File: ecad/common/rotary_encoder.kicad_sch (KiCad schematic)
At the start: 7 parts, among them Q1 RE1C002UN, SW1 PEL12T, U1 TLC5973

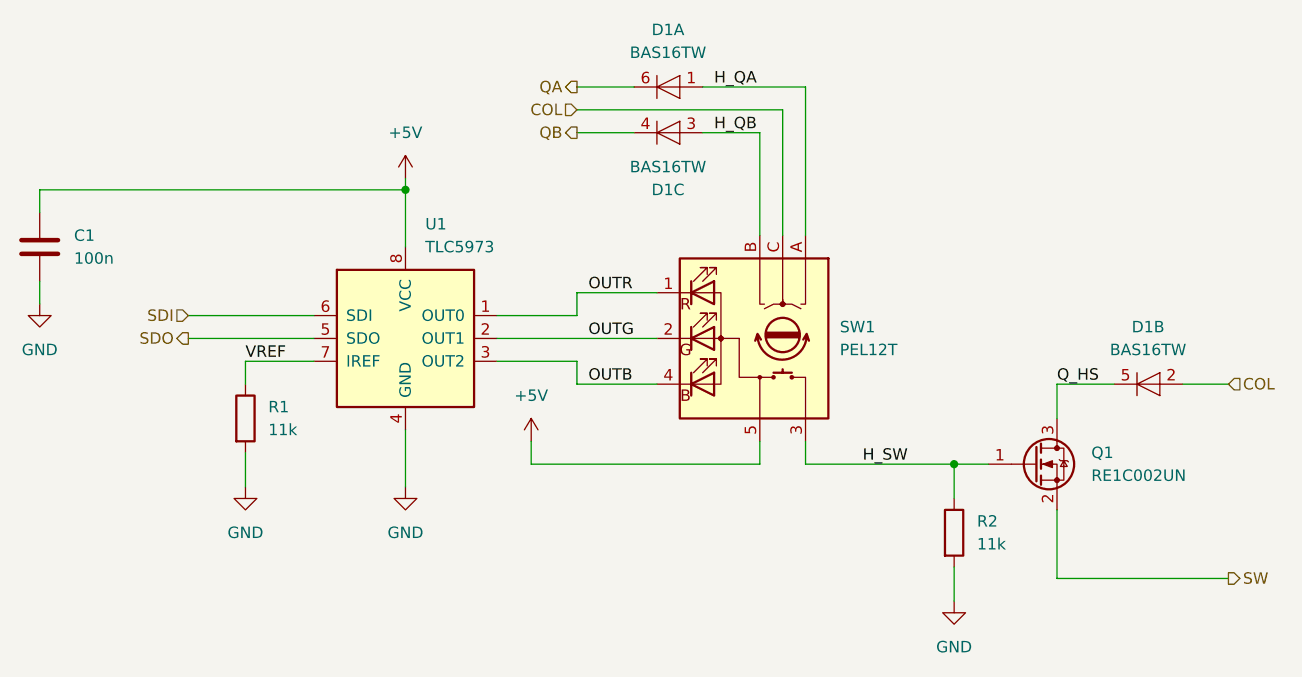
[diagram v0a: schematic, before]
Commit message: Draft a slightly smaller top board
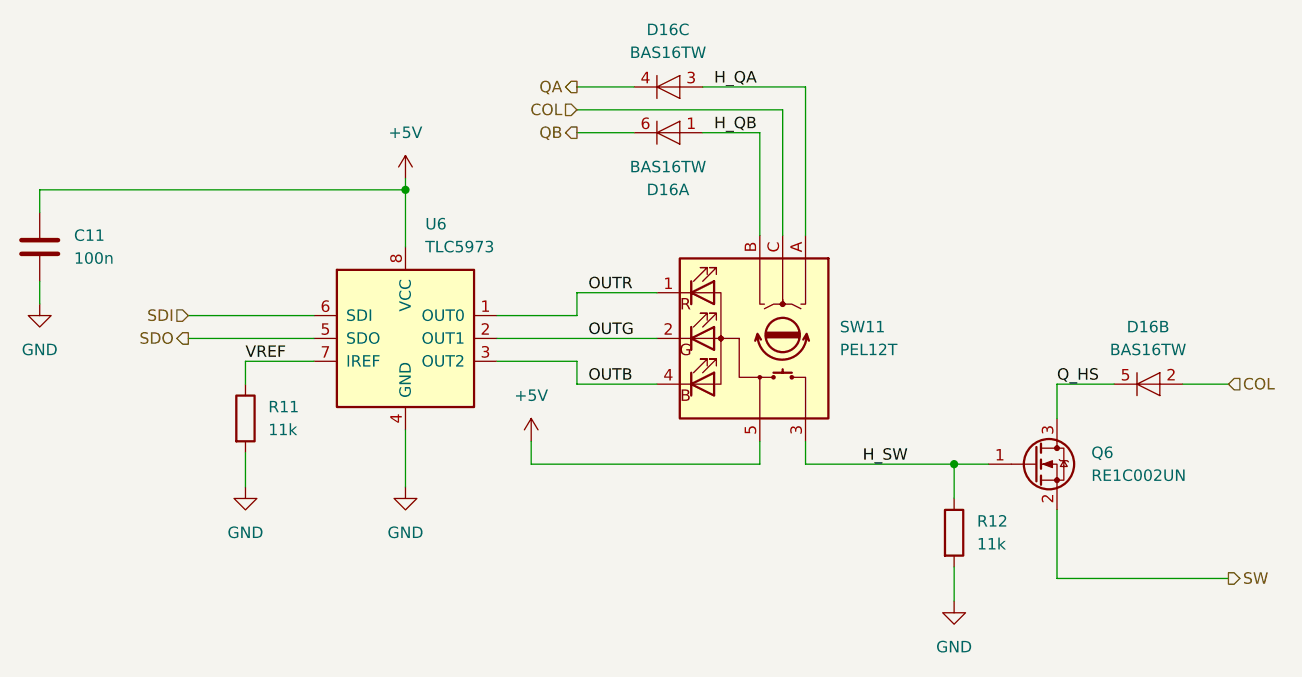
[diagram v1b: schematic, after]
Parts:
- renumbered C1 to C11, D1 to D16, Q1 to Q6, R1 to R11, R2 to R12, SW1 to SW11, U1 to U6
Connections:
- net H_QA: now also D16.3 (A); no longer D16.1 (A)
- net H_QB: now also D16.1 (A); no longer D16.3 (A)
- net QA: now also D16.4 (K); no longer D16.6 (K)
- net QB: now also D16.6 (K); no longer D16.4 (K)
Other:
- moved on the sheet: D16A, D16C
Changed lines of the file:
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@@
 	(symbol
 		(lib_id "Diode:BAS16TW")
-		(at 101.6 30.48 0)
-		(mirror x)
+		(at 101.6 25.4 0)
 		(unit 3)
 		(exclude_from_sim no)
@@
 		(on_board yes)
 		(dnp no)
-		(property "Reference" "D1"
-			(at 101.5619 36.83 0)
+		(property "Reference" "D16"
+			(at 101.5619 19.05 0)
 			(effects
 				(font
@@
 		)
 		(property "Value" "BAS16TW"
-			(at 101.5619 34.29 0)
+			(at 101.5619 21.59 0)
 			(effects
 				(font
@@
 		)
 		(property "Footprint" "Package_TO_SOT_SMD:SOT-363_SC-70-6"
-			(at 101.6 26.035 0)
+			(at 101.6 29.845 0)
 			(effects
 				(font
@@
 		)
 		(property "Datasheet" "http://www.diodes.com/datasheets/ds30154.pdf"
-			(at 101.6 33.02 0)
+			(at 101.6 22.86 0)
 			(effects
 				(font
@@
 		)
 		(property "Description" "Fast switching diode array 3 independent"
-			(at 101.6 30.48 0)
+			(at 101.6 25.4 0)
 			(effects
 				(font
@@
 		(dnp no)
 		(fields_autoplaced yes)
-		(property "Reference" "Q1"
+		(property "Reference" "Q6"
 			(at 148.59 66.04 0)
 			(effects
@@
 		(dnp no)
 		(fields_autoplaced yes)
-		(property "Reference" "#PWR05"
+		(property "Reference" "#PWR050"
 			(at 86.36 68.58 0)
 			(effects
@@
 		(dnp no)
 		(fields_autoplaced yes)
-		(property "Reference" "#PWR02"
+		(property "Reference" "#PWR047"
 			(at 54.61 76.2 0)
 			(effects
@@
 		(dnp no)
 		(fields_autoplaced yes)
-		(property "Reference" "SW1"
+		(property "Reference" "SW11"
 			(at 120.65 52.0699 90)
 			(effects
@@
 		(dnp no)
 		(fields_autoplaced yes)
-		(property "Reference" "U1"
+		(property "Reference" "U6"
 			(at 74.5841 40.64 0)
 			(effects
@@
 		(dnp no)
 		(fields_autoplaced yes)
-		(property "Reference" "#PWR04"
+		(property "Reference" "#PWR049"
 			(at 72.39 76.2 0)
 			(effects
@@
 		(dnp no)
 		(fields_autoplaced yes)
-		(property "Reference" "R2"
+		(property "Reference" "R12"
 			(at 135.89 73.6599 0)
 			(effects
@@
 		(dnp no)
 		(fields_autoplaced yes)
-		(property "Reference" "#PWR06"
+		(property "Reference" "#PWR051"
 			(at 133.35 88.9 0)
 			(effects
@@
 		(dnp no)
 		(fields_autoplaced yes)
-		(property "Reference" "C1"
+		(property "Reference" "C11"
 			(at 35.56 41.9099 0)
 			(effects
@@
 		(dnp no)
 		(fields_autoplaced yes)
-		(property "Reference" "R1"
+		(property "Reference" "R11"
 			(at 57.15 60.9599 0)
 			(effects
@@
 	(symbol
 		(lib_id "Diode:BAS16TW")
-		(at 101.6 25.4 0)
+		(at 101.6 30.48 0)
+		(mirror x)
 		(unit 1)
 		(exclude_from_sim no)
@@
 		(on_board yes)
 		(dnp no)
-		(property "Reference" "D1"
-			(at 101.5619 19.05 0)
+		(property "Reference" "D16"
+			(at 101.5619 36.83 0)
 			(effects
 				(font
@@
 		)
 		(property "Value" "BAS16TW"
-			(at 101.5619 21.59 0)
+			(at 101.5619 34.29 0)
 			(effects
 				(font
@@
 		)
 		(property "Footprint" "Package_TO_SOT_SMD:SOT-363_SC-70-6"
-			(at 101.6 29.845 0)
+			(at 101.6 26.035 0)
 			(effects
 				(font
@@
 		)
 		(property "Datasheet" "http://www.diodes.com/datasheets/ds30154.pdf"
-			(at 101.6 22.86 0)
+			(at 101.6 33.02 0)
 			(effects
 				(font
@@
 		)
 		(property "Description" "Fast switching diode array 3 independent"
-			(at 101.6 25.4 0)
+			(at 101.6 30.48 0)
 			(effects
 				(font
@@
 		(dnp no)
 		(fields_autoplaced yes)
-		(property "Reference" "D1"
+		(property "Reference" "D16"
 			(at 154.9019 52.07 0)
 			(effects
@@
 		(dnp no)
 		(fields_autoplaced yes)
-		(property "Reference" "#PWR01"
+		(property "Reference" "#PWR046"
 			(at 31.75 55.88 0)
 			(effects
@@
 		(dnp no)
 		(fields_autoplaced yes)
-		(property "Reference" "#PWR033"
+		(property "Reference" "#PWR048"
 			(at 72.39 39.37 0)
 			(effects
